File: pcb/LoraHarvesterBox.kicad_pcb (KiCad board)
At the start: 4 copper layers, 48 x 45.5 mm, 42 parts, among them J1 Conn_01x04_Socket, J2 Conn_01x02_Pin, J3 Conn_01x04_Socket, J4 Conn_01x02_Pin, J5 Conn_01x04_Socket, J6 Conn_01x04_Socket, J7 Conn_01x02_Pin, J8 Conn_01x06_Socket, SW1 TS-1088-AR02016, SW2 SSSS811101, U1 RAK3172-8-SM-I, U2 BQ25570, U3 FM24V10-GTR_C466851

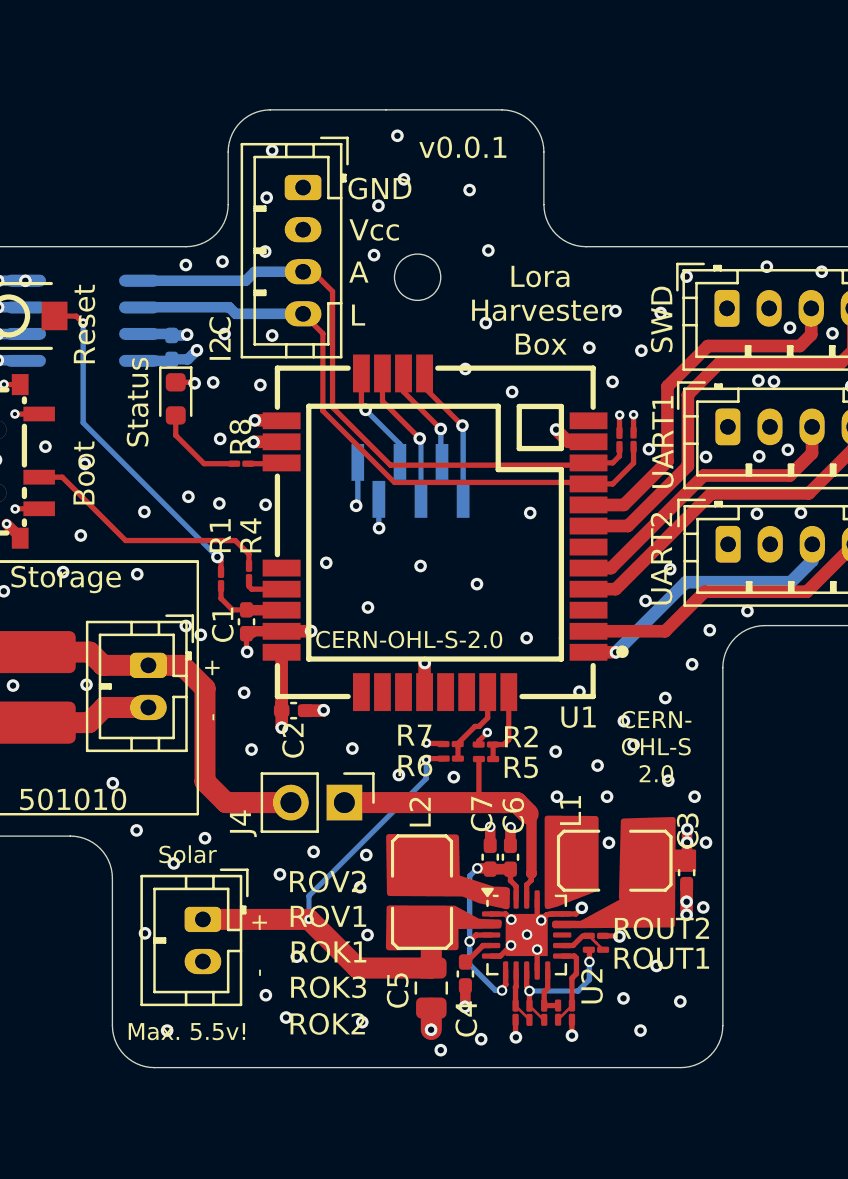
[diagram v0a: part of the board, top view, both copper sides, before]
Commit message: pcb: reannotate as the ROK names jumped around (1->3->2)
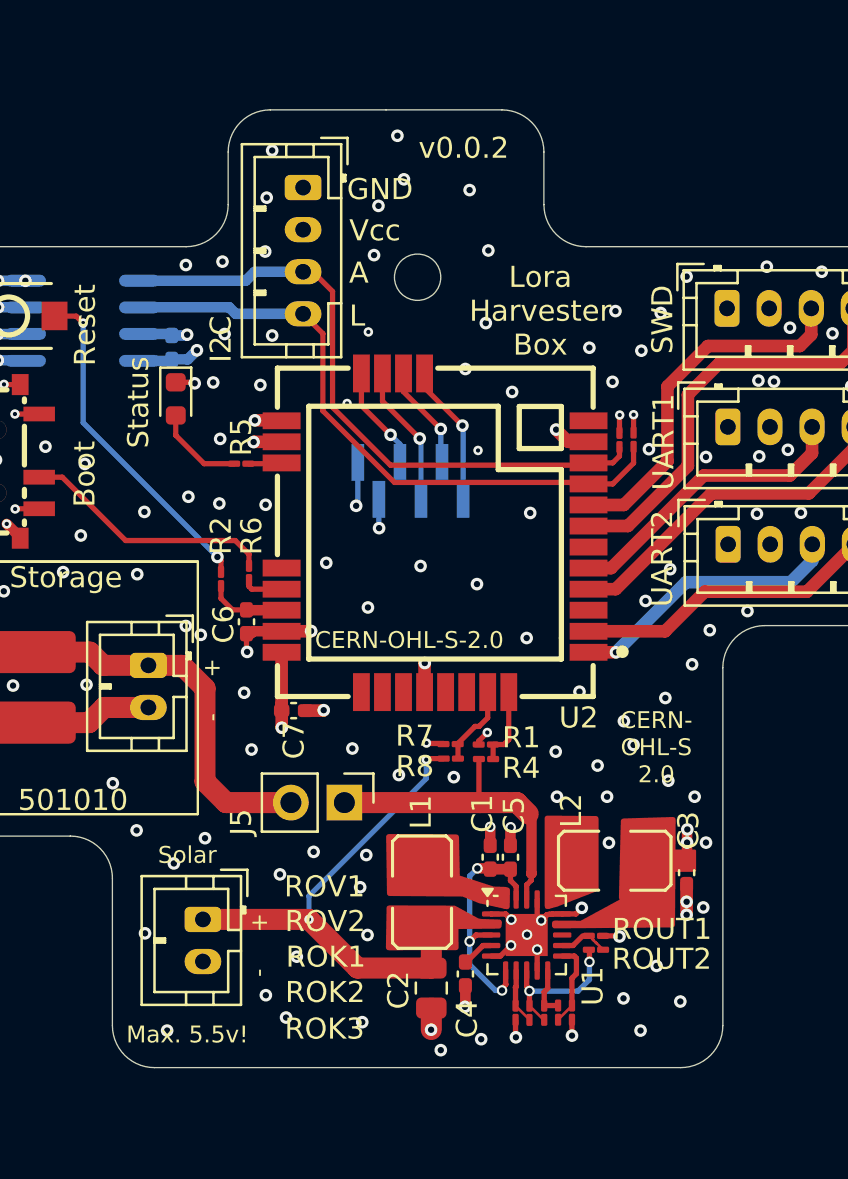
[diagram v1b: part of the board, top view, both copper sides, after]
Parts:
- renumbered C7 to C1, C5 to C2, C6 to C5, C1 to C6, C2 to C7, J7 to J1, J3 to J2, J5 to J3, J6 to J4, J4 to J5, J2 to J6, J1 to J7, L2 to L1, L1 to L2, R2 to R1, R1 to R2, R5 to R4, R8 to R5, R4 to R6, R6 to R8, ROK3 to ROK2, ROK2 to ROK3, ROUT2 to ROUT1, ROUT1 to ROUT2, ROV2 to ROV1, ROV1 to ROV2, U2 to U1, U1 to U2
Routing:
- net GND: vias 154 -> 157
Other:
- board text added: "v0.0.2"
- board text removed: "v0.0.1"

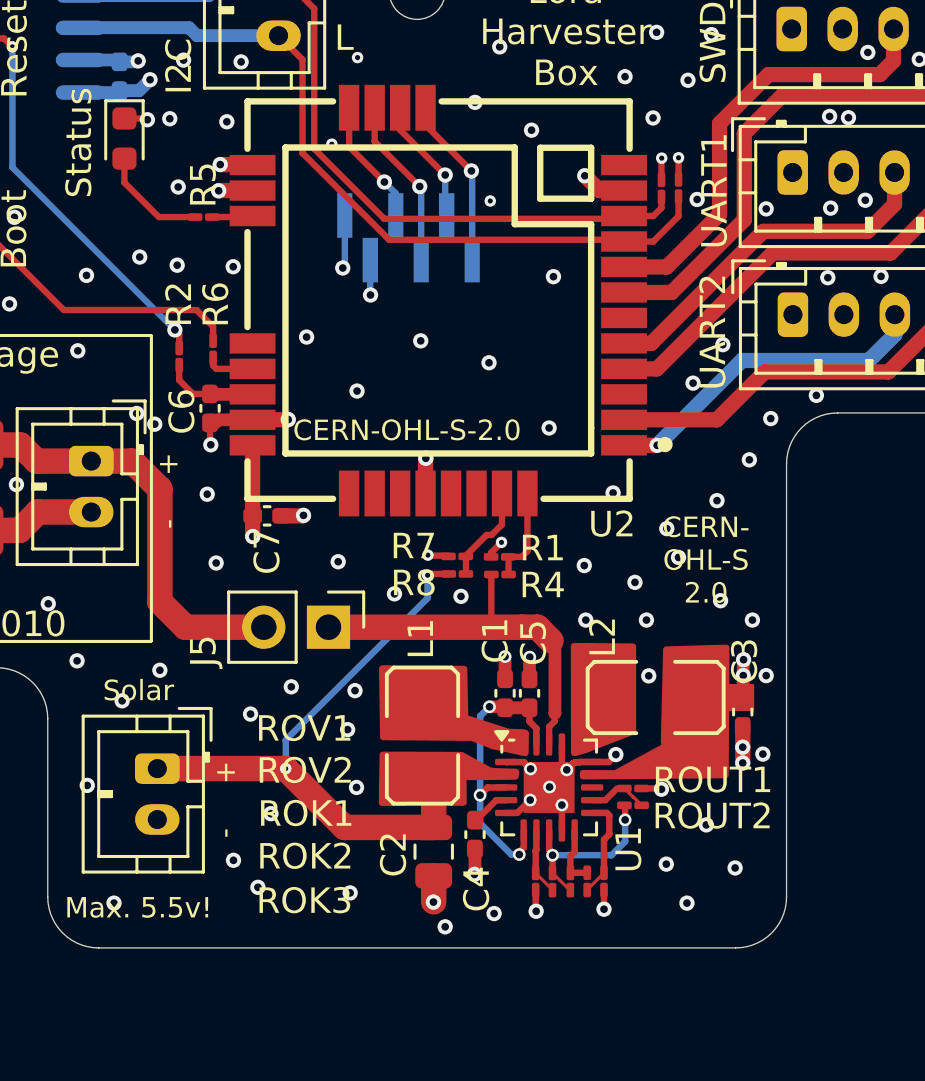
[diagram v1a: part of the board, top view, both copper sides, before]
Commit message: docs, sch, pcb: yes.. now we lost schematic<->datasheet sync. fix annotation
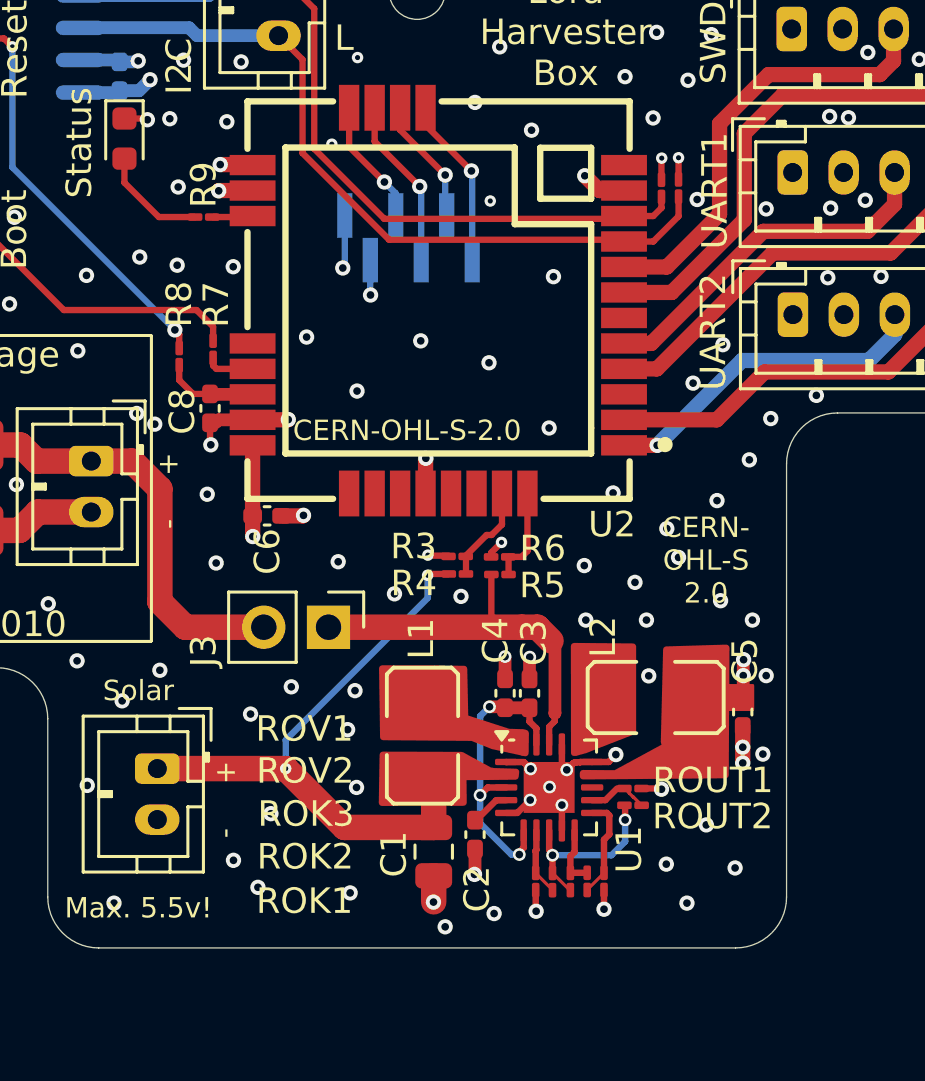
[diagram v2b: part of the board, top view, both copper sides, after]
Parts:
- renumbered C2 to C1, C4 to C2, C5 to C3, C1 to C4, C3 to C5, C7 to C6, C8 to C7, C6 to C8, J6 to J2, J5 to J3, J3 to J5, J2 to J6, R9 to R1, R3 to R2, R7 to R3, R8 to R4, R4 to R5, R1 to R6, R6 to R7, R2 to R8, R5 to R9, ROK3 to ROK1, ROK1 to ROK3, SW2 to SW1, SW1 to SW2
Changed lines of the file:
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@@
 		(descr "JST PH series connector, B4B-PH-K (http://www.jst-mfg.com/product/pdf/eng/ePH.pdf), generated with kicad-footprint-generator")
 		(tags "connector JST PH vertical")
-		(property "Reference" "J3"
+		(property "Reference" "J5"
 			(at -3.01 0.9 90)
 			(layer "F.SilkS")
@@
 		(descr "Resistor SMD 01005 (0402 Metric), square (rectangular) end terminal, IPC-7351 nominal with elongated pad for handsoldering. (Body size source: http://www.vishay.com/docs/20056/crcw01005e3.pdf), generated with kicad-footprint-generator")
 		(tags "resistor handsolder")
-		(property "Reference" "R2"
+		(property "Reference" "R8"
 			(at -2.0575 0 90)
 			(layer "F.SilkS")
@@
 		(descr "Resistor SMD 01005 (0402 Metric), square (rectangular) end terminal, IPC-7351 nominal with elongated pad for handsoldering. (Body size source: http://www.vishay.com/docs/20056/crcw01005e3.pdf), generated with kicad-footprint-generator")
 		(tags "resistor handsolder")
-		(property "Reference" "ROK3"
+		(property "Reference" "ROK1"
 			(at 0.7725 11.75375 0)
 			(layer "F.SilkS")
@@
 		(descr "Resistor SMD 01005 (0402 Metric), square (rectangular) end terminal, IPC-7351 nominal with elongated pad for handsoldering. (Body size source: http://www.vishay.com/docs/20056/crcw01005e3.pdf), generated with kicad-footprint-generator")
 		(tags "resistor handsolder")
-		(property "Reference" "R5"
+		(property "Reference" "R9"
 			(at 0 1.27 90)
 			(layer "F.SilkS")
@@
 		(descr "Resistor SMD 01005 (0402 Metric), square (rectangular) end terminal, IPC-7351 nominal with elongated pad for handsoldering. (Body size source: http://www.vishay.com/docs/20056/crcw01005e3.pdf), generated with kicad-footprint-generator")
 		(tags "resistor handsolder")
-		(property "Reference" "R6"
+		(property "Reference" "R7"
 			(at -1.76 -0.12 90)
 			(layer "F.SilkS")
@@
 		(descr "Capacitor SMD 0402 (1005 Metric), square (rectangular) end terminal, IPC-7351 nominal with elongated pad for handsoldering. (Body size source: IPC-SM-782 page 76, https://www.pcb-3d.com/wordpress/wp-content/uploads/ipc-sm-782a_amendment_1_and_2.pdf), generated with kicad-footprint-generator")
 		(tags "capacitor handsolder")
-		(property "Reference" "C5"
+		(property "Reference" "C3"
 			(at 1.98625 0.17 90)
 			(layer "F.SilkS")
@@
 		(descr "Capacitor SMD 0402 (1005 Metric), square (rectangular) end terminal, IPC-7351 nominal with elongated pad for handsoldering. (Body size source: IPC-SM-782 page 76, https://www.pcb-3d.com/wordpress/wp-content/uploads/ipc-sm-782a_amendment_1_and_2.pdf), generated with kicad-footprint-generator")
 		(tags "capacitor handsolder")
-		(property "Reference" "C4"
+		(property "Reference" "C2"
 			(at 2.13875 -0.08 90)
 			(layer "F.SilkS")
@@
 		(descr "Capacitor SMD 0402 (1005 Metric), square (rectangular) end terminal, IPC-7351 nominal with elongated pad for handsoldering. (Body size source: IPC-SM-782 page 76, https://www.pcb-3d.com/wordpress/wp-content/uploads/ipc-sm-782a_amendment_1_and_2.pdf), generated with kicad-footprint-generator")
 		(tags "capacitor handsolder")
-		(property "Reference" "C7"
+		(property "Reference" "C6"
 			(at -0.01 -1.4 90)
 			(layer "F.SilkS")
@@
 		(descr "Resistor SMD 01005 (0402 Metric), square (rectangular) end terminal, IPC-7351 nominal with elongated pad for handsoldering. (Body size source: http://www.vishay.com/docs/20056/crcw01005e3.pdf), generated with kicad-footprint-generator")
 		(tags "resistor handsolder")
-		(property "Reference" "R7"
+		(property "Reference" "R3"
 			(at 1.7075 0.39 0)
 			(layer "F.SilkS")
@@
 		(descr "Resistor SMD 01005 (0402 Metric), square (rectangular) end terminal, IPC-7351 nominal with elongated pad for handsoldering. (Body size source: http://www.vishay.com/docs/20056/crcw01005e3.pdf), generated with kicad-footprint-generator")
 		(tags "resistor handsolder")
-		(property "Reference" "R8"
+		(property "Reference" "R4"
 			(at -1.7075 0.37 0)
 			(layer "F.SilkS")
@@
 		(descr "Resistor SMD 01005 (0402 Metric), square (rectangular) end terminal, IPC-7351 nominal with elongated pad for handsoldering. (Body size source: http://www.vishay.com/docs/20056/crcw01005e3.pdf), generated with kicad-footprint-generator")
 		(tags "resistor handsolder")
-		(property "Reference" "R4"
+		(property "Reference" "R5"
 			(at 1.67 0.43 0)
 			(layer "F.SilkS")
@@
 		(descr "Resistor SMD 01005 (0402 Metric), square (rectangular) end terminal, IPC-7351 nominal with elongated pad for handsoldering. (Body size source: http://www.vishay.com/docs/20056/crcw01005e3.pdf), generated with kicad-footprint-generator")
 		(tags "resistor handsolder")
-		(property "Reference" "R9"
+		(property "Reference" "R1"
 			(at 0 -1 90)
 			(layer "F.SilkS")
@@
 		(descr "Capacitor SMD 0402 (1005 Metric), square (rectangular) end terminal, IPC-7351 nominal with elongated pad for handsoldering. (Body size source: IPC-SM-782 page 76, https://www.pcb-3d.com/wordpress/wp-content/uploads/ipc-sm-782a_amendment_1_and_2.pdf), generated with kicad-footprint-generator")
 		(tags "capacitor handsolder")
-		(property "Reference" "C1"
+		(property "Reference" "C4"
 			(at 2.07375 -0.37 90)
 			(layer "F.SilkS")
@@
 		(descr "Through hole straight pin header, 1x02, 2.54mm pitch, single row")
 		(tags "Through hole pin header THT 1x02 2.54mm single row")
-		(property "Reference" "J5"
+		(property "Reference" "J3"
 			(at 0.93 4.9 90)
 			(layer "F.SilkS")
@@
 		(layer "F.Cu")
 		(at 104.97 71.2 -90)
-		(property "Reference" "SW2"
+		(property "Reference" "SW1"
 			(at -4.91 0.4 0)
 			(layer "F.SilkS")
@@
 		(layer "F.Cu")
 		(at 105.07 64.29)
-		(property "Reference" "SW1"
+		(property "Reference" "SW2"
 			(at 0 -4 0)
 			(layer "F.SilkS")
@@
 		(descr "JST PH series connector, B2B-PH-K (http://www.jst-mfg.com/product/pdf/eng/ePH.pdf), generated with kicad-footprint-generator")
 		(tags "connector JST PH vertical")
-		(property "Reference" "J6"
+		(property "Reference" "J2"
 			(at 1 -2.9 90)
 			(layer "F.SilkS")
@@
 		(descr "Resistor SMD 01005 (0402 Metric), square (rectangular) end terminal, IPC-7351 nominal with elongated pad for handsoldering. (Body size source: http://www.vishay.com/docs/20056/crcw01005e3.pdf), generated with kicad-footprint-generator")
 		(tags "resistor handsolder")
-		(property "Reference" "R3"
+		(property "Reference" "R2"
 			(at 0 -1 90)
 			(layer "F.SilkS")
@@
 		(descr "JST PH series connector, B4B-PH-K (http://www.jst-mfg.com/product/pdf/eng/ePH.pdf), generated with kicad-footprint-generator")
 		(tags "connector JST PH vertical")
-		(property "Reference" "J2"
+		(property "Reference" "J6"
 			(at -3.06 0.76 90)
 			(layer "F.SilkS")
@@
 		(descr "Capacitor SMD 0805 (2012 Metric), square (rectangular) end terminal, IPC-7351 nominal, (Body size source: IPC-SM-782 page 76, https://www.pcb-3d.com/wordpress/wp-content/uploads/ipc-sm-782a_amendment_1_and_2.pdf, https://docs.google.com/spreadsheets/d/1BsfQQcO9C6DZCsRaXUlFlo91Tg2WpOkGARC1WS5S8t0/edit?usp=sharing), generated with kicad-footprint-generator")
 		(tags "capacitor")
-		(property "Reference" "C2"
+		(property "Reference" "C1"
 			(at 0.1 1.56 270)
 			(layer "F.SilkS")
@@
 		(descr "Capacitor SMD 0402 (1005 Metric), square (rectangular) end terminal, IPC-7351 nominal with elongated pad for handsoldering. (Body size source: IPC-SM-782 page 76, https://www.pcb-3d.com/wordpress/wp-content/uploads/ipc-sm-782a_amendment_1_and_2.pdf), generated with kicad-footprint-generator")
 		(tags "capacitor handsolder")
-		(property "Reference" "C3"
+		(property "Reference" "C5"
 			(at 2.01 0.09 90)
 			(layer "F.SilkS")
@@
 		(descr "Resistor SMD 01005 (0402 Metric), square (rectangular) end terminal, IPC-7351 nominal with elongated pad for handsoldering. (Body size source: http://www.vishay.com/docs/20056/crcw01005e3.pdf), generated with kicad-footprint-generator")
 		(tags "resistor handsolder")
-		(property "Reference" "ROK1"
+		(property "Reference" "ROK3"
 			(at 2.6525 -10.37375 0)
 			(layer "F.SilkS")
@@
 		(descr "Capacitor SMD 0402 (1005 Metric), square (rectangular) end terminal, IPC-7351 nominal with elongated pad for handsoldering. (Body size source: IPC-SM-782 page 76, https://www.pcb-3d.com/wordpress/wp-content/uploads/ipc-sm-782a_amendment_1_and_2.pdf), generated with kicad-footprint-generator")
 		(tags "capacitor handsolder")
-		(property "Reference" "C6"
+		(property "Reference" "C8"
 			(at 0.12 1.09 90)
 			(layer "F.SilkS")
@@
 		(descr "Resistor SMD 01005 (0402 Metric), square (rectangular) end terminal, IPC-7351 nominal with elongated pad for handsoldering. (Body size source: http://www.vishay.com/docs/20056/crcw01005e3.pdf), generated with kicad-footprint-generator")
 		(tags "resistor handsolder")
-		(property "Reference" "R1"
+		(property "Reference" "R6"
 			(at -1.69 0.33 0)
 			(layer "F.SilkS")
@@
 		(descr "Capacitor SMD 0402 (1005 Metric), square (rectangular) end terminal, IPC-7351 nominal with elongated pad for handsoldering. (Body size source: IPC-SM-782 page 76, https://www.pcb-3d.com/wordpress/wp-content/uploads/ipc-sm-782a_amendment_1_and_2.pdf), generated with kicad-footprint-generator")
 		(tags "capacitor handsolder")
-		(property "Reference" "C8"
+		(property "Reference" "C7"
 			(at 0.075 -1.2 90)
 			(layer "B.SilkS")
